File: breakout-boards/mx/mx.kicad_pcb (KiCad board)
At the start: 2 copper layers, 22.9 x 33 mm, 10 parts, among them J1 CONN_PWR, J2 CONN_KEYSW, J3 CONN_LED, U1 keyswitch_mx

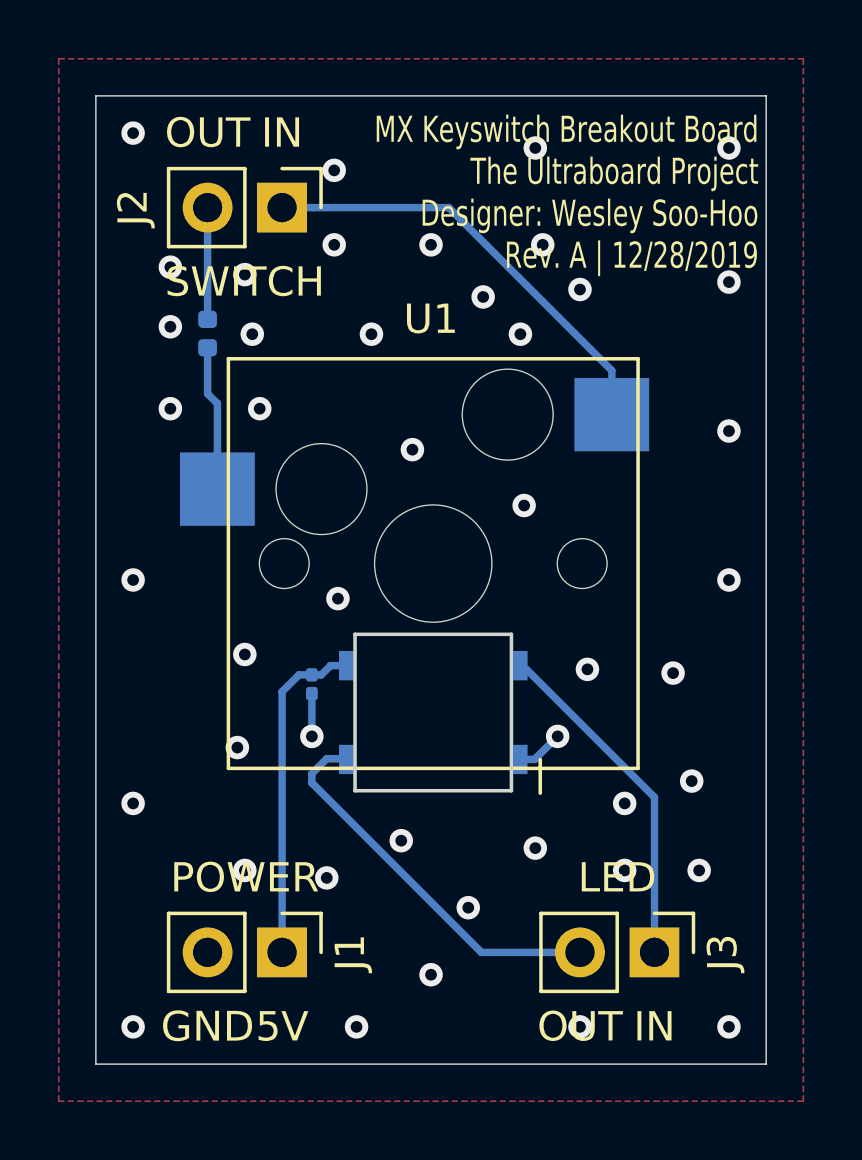
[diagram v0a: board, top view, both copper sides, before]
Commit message: (#6) updated mx breakout board to use 3535 led
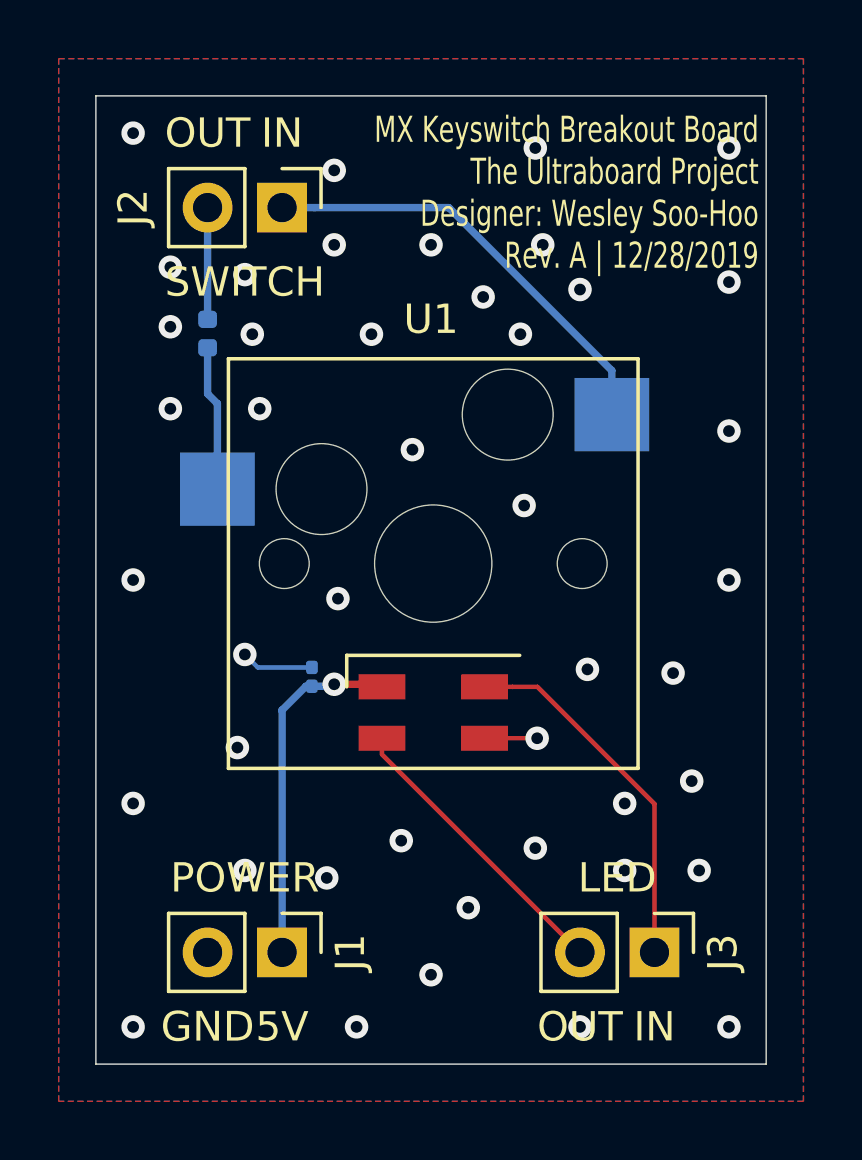
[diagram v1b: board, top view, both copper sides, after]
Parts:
- moved C1 0.25 mm to (130.6, 122.7), turned to 270 degrees
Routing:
- net /LED_DOUT: track 13.2 -> 10.1 mm
- net GND: track 2.97 -> 4.26 mm, vias 45 -> 44
- net /LED_DIN: track 11.6 -> 12.5 mm
- net +5V: track 11.4 -> 12.1 mm, vias 0 -> 1

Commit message: (#16) fix footprints for diode and cap, create gerbers and bom
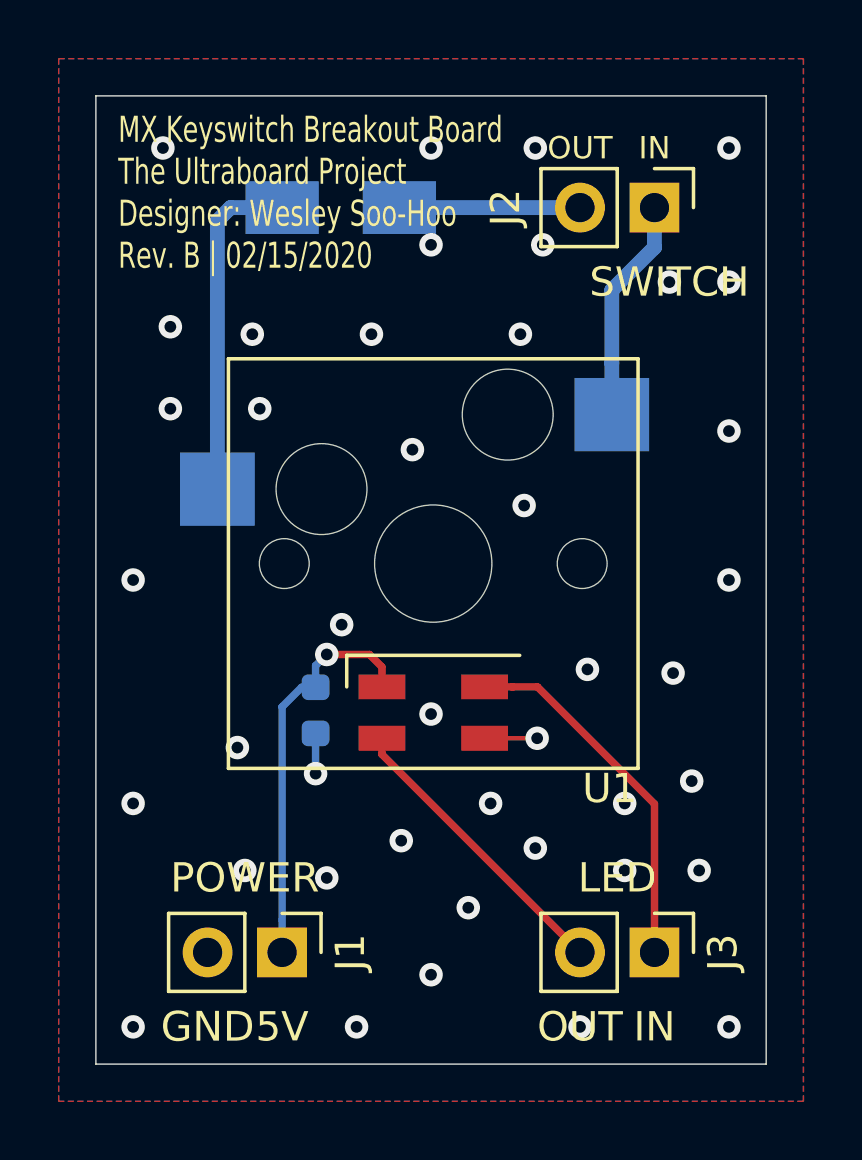
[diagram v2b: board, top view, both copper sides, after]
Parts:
- removed G***: LOGO, ultraboard-img:surprised_pika
- removed G***: LOGO, ultraboard-img:saltbae
- removed G***: LOGO, ultraboard-img:minion
- removed G***: LOGO, ultraboard-img:michael_scott
- C1: value 0.1uF -> C_100nF; footprint Capacitor_SMD:C_0201_0603Metric -> Capacitor_SMD:C_0603_1608Metric
- D1: footprint Diode_SMD:D_0402_1005Metric -> Diode_SMD:D_SMA
- moved J2 12.7 mm to (142.2, 106.7)
- moved D1 6.25 mm to (131.5, 106.7), turned to 180 degrees
- moved C1 1.15 mm to (130.7, 123.8), turned to 90 degrees
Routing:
- net /KEYSW_IN: track 15.1 -> 7.66 mm
- net Net-(D1-Pad2): track 4.96 -> 11.5 mm
- net /KEYSW_OUT: track 3.81 -> 6.16 mm
- net +5V: track 12.1 -> 13.8 mm
- net GND: track 4.26 -> 3.17 mm, vias 44 -> 42
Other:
- board text added: "MX Keyswitch Breakout Board The Ultraboard Project Designer: Wesley Soo-Hoo Rev. B | 02/15/2020"
- board text removed: "MX Keyswitch Breakout Board The Ultraboard Project Designer: Wesley Soo-Hoo Rev. A | 12/28/2019"
